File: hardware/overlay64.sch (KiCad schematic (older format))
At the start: 16 parts, among them IC1 ATMEGA328P-P, P1 ISP, P2 MAIN, P3 INPUT/BYPASS, Q1 BC547B, U1 LM1881, Y1 20MHz

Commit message: Hardware: Added jumper for backdrop (decreased luminance as background)
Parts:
- added JP1: BACKDROP, symbol JUMPER
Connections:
- wire segments 26 -> 27
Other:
- moved on the sheet: R2, RV1
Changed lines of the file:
@@
 L POT RV1
 U 1 1 56A8F98B
-P 5800 3150
-F 0 "RV1" H 5800 3050 50  0000 C CNN
-F 1 "1k" H 5800 3150 50  0000 C CNN
-F 2 "Potentiometers:Potentiometer_Bourns_3339H_Angular_ScrewUp" H 5800 3150 60  0001 C CNN
-F 3 "" H 5800 3150 60  0000 C CNN
-	1    5800 3150
-	1    0    0    -1
-$EndComp
-NoConn ~ 6050 3150
+P 5800 3350
+F 0 "RV1" H 5800 3250 50  0000 C CNN
+F 1 "1k" H 5800 3350 50  0000 C CNN
+F 2 "Potentiometers:Potentiometer_Bourns_3339H_Angular_ScrewUp" H 5800 3350 60  0001 C CNN
+F 3 "" H 5800 3350 60  0000 C CNN
+	1    5800 3350
+	1    0    0    -1
+$EndComp
+NoConn ~ 6050 3350
 Text Label 4350 3950 0    60   ~ 0
 ~RESET
@@
 	4350 3250 4350 3200
 NoConn ~ 4350 2700
-Wire Wire Line
-	5550 3150 5550 3550
 Wire Wire Line
 	2350 2800 2450 2800
@@
 L R R2
 U 1 1 56AA9AFF
-P 5250 2800
-F 0 "R2" V 5330 2800 50  0000 C CNN
-F 1 "4k7" V 5250 2800 50  0000 C CNN
-F 2 "" V 5180 2800 50  0000 C CNN
-F 3 "" H 5250 2800 50  0000 C CNN
-	1    5250 2800
+P 5350 2800
+F 0 "R2" V 5430 2800 50  0000 C CNN
+F 1 "4k7" V 5350 2800 50  0000 C CNN
+F 2 "" V 5280 2800 50  0000 C CNN
+F 3 "" H 5350 2800 50  0000 C CNN
+	1    5350 2800
 	0    1    1    0
 $EndComp
 Wire Wire Line
-	4350 2800 5100 2800
-Wire Wire Line
-	5400 2800 5500 2800
+	4350 2800 5200 2800
 Text Label 4350 4800 0    60   ~ 0
 ~OE
@@
 Text Label 8250 4300 0    60   ~ 0
 IN12
+$Comp
+L JUMPER JP1
+U 1 1 56B2539D
+P 5500 3100
+F 0 "JP1" H 5500 3250 50  0000 C CNN
+F 1 "BACKDROP" H 5500 3020 50  0000 C CNN
+F 2 "" H 5500 3100 50  0000 C CNN
+F 3 "" H 5500 3100 50  0000 C CNN
+	1    5500 3100
+	1    0    0    -1
+$EndComp
+Wire Wire Line
+	5800 3000 5800 3200
+Connection ~ 5800 3100
+Wire Wire Line
+	5550 3350 5550 3550
+Wire Wire Line
+	5200 2800 5200 3100
 $EndSCHEMATC

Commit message: Hardware: First draft of pcb layout (rough)
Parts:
- removed Q1: BC547B, TO_SOT_Packages_THT:TO-92_Inline_Narrow_Oval, symbol Q_NPN_BCE
- added Q1: BC547B, TO_SOT_Packages_THT:TO-92_Inline_Narrow_Oval, symbol BC547
- JP1: footprint (none) -> Pin_Headers:Pin_Header_Straight_1x02
- R2: footprint (none) -> Discret:R1
- RV1: footprint Potentiometers:Potentiometer_Bourns_3339H_Angular_ScrewUp -> Potentiometers:Potentiometer_Bourns_3339P_Angular_ScrewUp
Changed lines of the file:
@@
 $EndComp
 $Comp
-L PWR_FLAG #FLG01
+L PWR_FLAG #FLG1
 U 1 1 56A1EF0B
 P 6250 7500
-F 0 "#FLG01" H 6250 7595 50  0001 C CNN
+F 0 "#FLG1" H 6250 7595 50  0001 C CNN
 F 1 "PWR_FLAG" H 6250 7680 50  0000 C CNN
 F 2 "" H 6250 7500 60  0000 C CNN
@@
 $EndComp
 $Comp
-L VCC #PWR02
+L VCC #PWR12
 U 1 1 56A1EF40
 P 6250 7500
-F 0 "#PWR02" H 6250 7350 50  0001 C CNN
+F 0 "#PWR12" H 6250 7350 50  0001 C CNN
 F 1 "VCC" H 6250 7650 50  0000 C CNN
 F 2 "" H 6250 7500 60  0000 C CNN
@@
 $EndComp
 $Comp
-L PWR_FLAG #FLG03
+L PWR_FLAG #FLG2
 U 1 1 56A1EF56
 P 6700 7500
-F 0 "#FLG03" H 6700 7595 50  0001 C CNN
+F 0 "#FLG2" H 6700 7595 50  0001 C CNN
 F 1 "PWR_FLAG" H 6700 7680 50  0000 C CNN
 F 2 "" H 6700 7500 60  0000 C CNN
@@
 $EndComp
 $Comp
-L GND #PWR04
+L GND #PWR15
 U 1 1 56A1EF6C
 P 6700 7500
-F 0 "#PWR04" H 6700 7250 50  0001 C CNN
+F 0 "#PWR15" H 6700 7250 50  0001 C CNN
 F 1 "GND" H 6700 7350 50  0000 C CNN
 F 2 "" H 6700 7500 60  0000 C CNN
@@
 $EndComp
 $Comp
-L VCC #PWR05
+L VCC #PWR9
 U 1 1 56A1F13D
 P 5600 4850
-F 0 "#PWR05" H 5600 4700 50  0001 C CNN
+F 0 "#PWR9" H 5600 4700 50  0001 C CNN
 F 1 "VCC" H 5600 5000 50  0000 C CNN
 F 2 "" H 5600 4850 60  0000 C CNN
@@
 $EndComp
 $Comp
-L GND #PWR06
+L GND #PWR10
 U 1 1 56A1F155
 P 5600 5150
-F 0 "#PWR06" H 5600 4900 50  0001 C CNN
+F 0 "#PWR10" H 5600 4900 50  0001 C CNN
 F 1 "GND" H 5600 5000 50  0000 C CNN
 F 2 "" H 5600 5150 60  0000 C CNN
@@
 $EndComp
 $Comp
-L GND #PWR07
+L GND #PWR2
 U 1 1 56A1F1BC
 P 2050 2800
-F 0 "#PWR07" H 2050 2550 50  0001 C CNN
+F 0 "#PWR2" H 2050 2550 50  0001 C CNN
 F 1 "GND" H 2050 2650 50  0000 C CNN
 F 2 "" H 2050 2800 60  0000 C CNN
@@
 $EndComp
 $Comp
-L GND #PWR08
+L GND #PWR16
 U 1 1 56A1F3BB
 P 6850 4350
-F 0 "#PWR08" H 6850 4100 50  0001 C CNN
+F 0 "#PWR16" H 6850 4100 50  0001 C CNN
 F 1 "GND" H 6850 4200 50  0000 C CNN
 F 2 "" H 6850 4350 60  0000 C CNN
@@
 $EndComp
 $Comp
-L VCC #PWR09
+L VCC #PWR1
 U 1 1 56A1FF3A
 P 2000 2500
-F 0 "#PWR09" H 2000 2350 50  0001 C CNN
+F 0 "#PWR1" H 2000 2350 50  0001 C CNN
 F 1 "VCC" H 2000 2650 50  0000 C CNN
 F 2 "" H 2000 2500 60  0000 C CNN
@@
 $EndComp
 $Comp
-L GND #PWR010
+L GND #PWR3
 U 1 1 56A20155
 P 2450 4700
-F 0 "#PWR010" H 2450 4450 50  0001 C CNN
+F 0 "#PWR3" H 2450 4450 50  0001 C CNN
 F 1 "GND" H 2450 4550 50  0000 C CNN
 F 2 "" H 2450 4700 60  0000 C CNN
@@
 $EndComp
 $Comp
-L GND #PWR011
+L GND #PWR4
 U 1 1 56A60DBD
 P 2450 4800
-F 0 "#PWR011" H 2450 4550 50  0001 C CNN
+F 0 "#PWR4" H 2450 4550 50  0001 C CNN
 F 1 "GND" H 2450 4650 50  0000 C CNN
 F 2 "" H 2450 4800 60  0000 C CNN
@@
 Connection ~ 6850 4350
 $Comp
-L Q_NPN_BCE Q1
-U 1 1 56A78043
-P 5700 2800
-F 0 "Q1" H 6000 2850 50  0000 R CNN
-F 1 "BC547B" H 6150 2750 50  0000 R CNN
-F 2 "TO_SOT_Packages_THT:TO-92_Inline_Narrow_Oval" H 5900 2900 29  0001 C CNN
-F 3 "" H 5700 2800 60  0000 C CNN
-	1    5700 2800
-	1    0    0    -1
-$EndComp
-$Comp
-L VCC #PWR012
+L VCC #PWR11
 U 1 1 56A78618
 P 5800 2600
-F 0 "#PWR012" H 5800 2450 50  0001 C CNN
+F 0 "#PWR11" H 5800 2450 50  0001 C CNN
 F 1 "VCC" H 5800 2750 50  0000 C CNN
 F 2 "" H 5800 2600 60  0000 C CNN
@@
 F 0 "RV1" H 5800 3250 50  0000 C CNN
 F 1 "1k" H 5800 3350 50  0000 C CNN
-F 2 "Potentiometers:Potentiometer_Bourns_3339H_Angular_ScrewUp" H 5800 3350 60  0001 C CNN
+F 2 "Potentiometers:Potentiometer_Bourns_3339P_Angular_ScrewUp" H 5800 3350 60  0001 C CNN
 F 3 "" H 5800 3350 60  0000 C CNN
 	1    5800 3350
@@
 MOSI
 $Comp
-L VCC #PWR013
+L VCC #PWR5
 U 1 1 56A92B5A
 P 3750 1750
-F 0 "#PWR013" H 3750 1600 50  0001 C CNN
+F 0 "#PWR5" H 3750 1600 50  0001 C CNN
 F 1 "VCC" H 3750 1900 50  0000 C CNN
 F 2 "" H 3750 1750 60  0000 C CNN
@@
 $EndComp
 $Comp
-L GND #PWR014
+L GND #PWR6
 U 1 1 56A92BBD
 P 3750 1950
-F 0 "#PWR014" H 3750 1700 50  0001 C CNN
+F 0 "#PWR6" H 3750 1700 50  0001 C CNN
 F 1 "GND" H 3750 1800 50  0000 C CNN
 F 2 "" H 3750 1950 60  0000 C CNN
@@
 $EndComp
 $Comp
-L GND #PWR015
+L GND #PWR7
 U 1 1 56A976F1
 P 4850 3050
-F 0 "#PWR015" H 4850 2800 50  0001 C CNN
+F 0 "#PWR7" H 4850 2800 50  0001 C CNN
 F 1 "GND" H 4850 2900 50  0000 C CNN
 F 2 "" H 4850 3050 60  0000 C CNN
@@
 $EndComp
 $Comp
-L GND #PWR016
+L GND #PWR8
 U 1 1 56A97733
 P 4850 3250
-F 0 "#PWR016" H 4850 3000 50  0001 C CNN
+F 0 "#PWR8" H 4850 3000 50  0001 C CNN
 F 1 "GND" H 4850 3100 50  0000 C CNN
 F 2 "" H 4850 3250 60  0000 C CNN
@@
 $EndComp
 $Comp
-L VCC #PWR017
+L VCC #PWR13
 U 1 1 56A9E7D0
 P 6450 3450
-F 0 "#PWR017" H 6450 3300 50  0001 C CNN
+F 0 "#PWR13" H 6450 3300 50  0001 C CNN
 F 1 "VCC" H 6450 3600 50  0000 C CNN
 F 2 "" H 6450 3450 60  0000 C CNN
@@
 $EndComp
 $Comp
-L GND #PWR018
+L GND #PWR14
 U 1 1 56A9E875
 P 6450 3650
-F 0 "#PWR018" H 6450 3400 50  0001 C CNN
+F 0 "#PWR14" H 6450 3400 50  0001 C CNN
 F 1 "GND" H 6450 3500 50  0000 C CNN
 F 2 "" H 6450 3650 60  0000 C CNN
@@
 F 0 "R2" V 5430 2800 50  0000 C CNN
 F 1 "4k7" V 5350 2800 50  0000 C CNN
-F 2 "" V 5280 2800 50  0000 C CNN
+F 2 "Discret:R1" V 5280 2800 50  0001 C CNN
 F 3 "" H 5350 2800 50  0000 C CNN
 	1    5350 2800
@@
 F 0 "JP1" H 5500 3250 50  0000 C CNN
 F 1 "BACKDROP" H 5500 3020 50  0000 C CNN
-F 2 "" H 5500 3100 50  0000 C CNN
+F 2 "Pin_Headers:Pin_Header_Straight_1x02" H 5500 3100 50  0001 C CNN
 F 3 "" H 5500 3100 50  0000 C CNN
 	1    5500 3100
@@
 Wire Wire Line
 	5200 2800 5200 3100
+$Comp
+L BC547 Q1
+U 1 1 56B5F1A8
+P 5700 2800
+F 0 "Q1" H 5900 2875 50  0000 L CNN
+F 1 "BC547B" H 5900 2800 50  0000 L CNN
+F 2 "TO_SOT_Packages_THT:TO-92_Inline_Narrow_Oval" H 5900 2725 50  0001 L CIN
+F 3 "" H 5700 2800 50  0000 L CNN
+	1    5700 2800
+	1    0    0    -1
+$EndComp
 $EndSCHEMATC

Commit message: Firmware: Added global output enable pin, improved control logic
The former OE (output enable) pin has been renamed to OR (output request)
and another pin has been introduced as OE (output enable).

The output enable pin now directly controls whether or not the display is
active. When low, the display is enabled. When going high again, the
display is immediately disabled, regardless of any running timeouts from a
former output request.

This allows using the OE line like a switch to turn the display on and off
while a low pulse on OR can be used to temporarily show the current state
for a certain time.
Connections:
- net IN12 is gone; now on net ~OE: IC1.12 ((PCINT22/OC0A/AIN0)PD6), P3.25 (P25), P3.26 (P26)
- net ~OE: no longer IC1.13 ((PCINT23/AIN1)PD7), P3.27 (P27), P3.28 (P28)
- new net ~OR: IC1.13 ((PCINT23/AIN1)PD7), P3.27 (P27), P3.28 (P28)
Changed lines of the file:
@@
 Text Label 4350 4600 0    60   ~ 0
 IN11
-Text Label 4350 4700 0    60   ~ 0
-IN12
 Wire Wire Line
 	5300 4350 5200 4350
@@
 Text Label 7750 4200 2    60   ~ 0
 IN11
-Text Label 7750 4300 2    60   ~ 0
-IN12
 $Comp
 L R R2
@@
 	4350 2800 5200 2800
 Text Label 4350 4800 0    60   ~ 0
-~OE
-Text Label 7750 4400 2    60   ~ 0
+~OR
+Text Label 7750 4300 2    60   ~ 0
 ~OE
 Text Label 6150 3550 0    60   ~ 0
@@
 	1    0    0    -1
 $EndComp
-Text Label 8250 4400 0    60   ~ 0
+Text Label 8250 4300 0    60   ~ 0
 ~OE
 Text Label 8250 3100 0    60   ~ 0
@@
 Text Label 8250 4200 0    60   ~ 0
 IN11
-Text Label 8250 4300 0    60   ~ 0
-IN12
 $Comp
 L JUMPER JP1
@@
 	1    0    0    -1
 $EndComp
+Text Label 4350 4700 0    60   ~ 0
+~OE
+Text Label 8250 4400 0    60   ~ 0
+~OR
+Text Label 7750 4400 2    60   ~ 0
+~OR
 $EndSCHEMATC

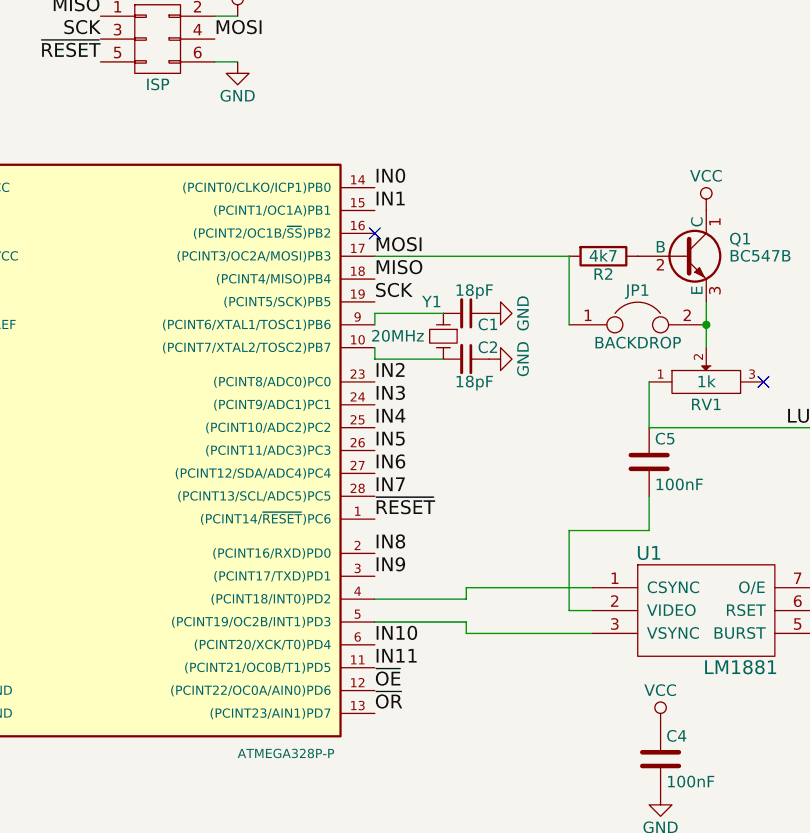
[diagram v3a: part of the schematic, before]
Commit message: Hardware: Adjusted input pin connections to new logical layout
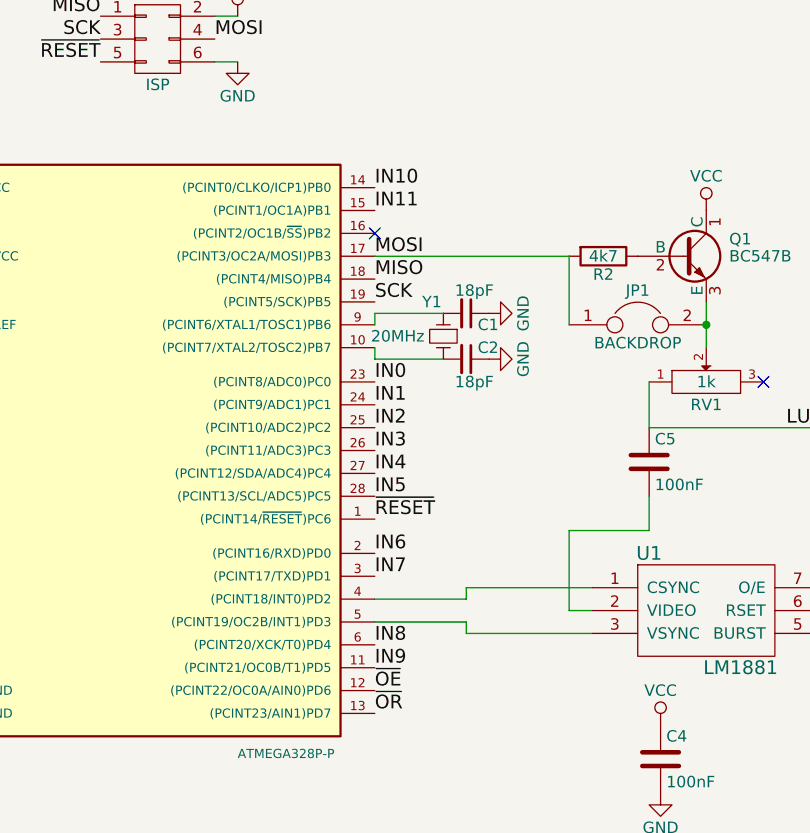
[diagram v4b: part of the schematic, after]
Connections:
- net IN0: now also IC1.23 ((PCINT8/ADC0)PC0); no longer IC1.14 ((PCINT0/CLKO/ICP1)PB0)
- net IN1: now also IC1.24 ((PCINT9/ADC1)PC1); no longer IC1.15 ((PCINT1/OC1A)PB1)
- net IN10: now also IC1.14 ((PCINT0/CLKO/ICP1)PB0); no longer IC1.6 ((PCINT20/XCK/T0)PD4)
- net IN11: now also IC1.15 ((PCINT1/OC1A)PB1); no longer IC1.11 ((PCINT21/OC0B/T1)PD5)
- net IN2: now also IC1.25 ((PCINT10/ADC2)PC2); no longer IC1.23 ((PCINT8/ADC0)PC0)
- net IN3: now also IC1.26 ((PCINT11/ADC3)PC3); no longer IC1.24 ((PCINT9/ADC1)PC1)
- net IN4: now also IC1.27 ((PCINT12/SDA/ADC4)PC4); no longer IC1.25 ((PCINT10/ADC2)PC2)
- net IN5: now also IC1.28 ((PCINT13/SCL/ADC5)PC5); no longer IC1.26 ((PCINT11/ADC3)PC3)
- net IN6: now also IC1.2 ((PCINT16/RXD)PD0); no longer IC1.27 ((PCINT12/SDA/ADC4)PC4)
- net IN7: now also IC1.3 ((PCINT17/TXD)PD1); no longer IC1.28 ((PCINT13/SCL/ADC5)PC5)
- net IN8: now also IC1.6 ((PCINT20/XCK/T0)PD4); no longer IC1.2 ((PCINT16/RXD)PD0)
- net IN9: now also IC1.11 ((PCINT21/OC0B/T1)PD5); no longer IC1.3 ((PCINT17/TXD)PD1)
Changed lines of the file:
@@
 	1    0    0    -1
 $EndComp
+Text Label 4350 3350 0    60   ~ 0
+IN0
+Text Label 4350 3450 0    60   ~ 0
+IN1
+Text Label 4350 3550 0    60   ~ 0
+IN2
+Text Label 4350 3650 0    60   ~ 0
+IN3
+Text Label 4350 3750 0    60   ~ 0
+IN4
+Text Label 4350 3850 0    60   ~ 0
+IN5
+Text Label 4350 4100 0    60   ~ 0
+IN6
+Text Label 4350 4200 0    60   ~ 0
+IN7
+Text Label 4350 4500 0    60   ~ 0
+IN8
+Text Label 4350 4600 0    60   ~ 0
+IN9
 Text Label 4350 2500 0    60   ~ 0
-IN0
+IN10
 Text Label 4350 2600 0    60   ~ 0
-IN1
-Text Label 4350 3350 0    60   ~ 0
-IN2
-Text Label 4350 3450 0    60   ~ 0
-IN3
-Text Label 4350 3550 0    60   ~ 0
-IN4
-Text Label 4350 3650 0    60   ~ 0
-IN5
-Text Label 4350 3750 0    60   ~ 0
-IN6
-Text Label 4350 3850 0    60   ~ 0
-IN7
-Text Label 4350 4100 0    60   ~ 0
-IN8
-Text Label 4350 4200 0    60   ~ 0
-IN9
-Text Label 4350 4500 0    60   ~ 0
-IN10
-Text Label 4350 4600 0    60   ~ 0
 IN11
 Wire Wire Line
